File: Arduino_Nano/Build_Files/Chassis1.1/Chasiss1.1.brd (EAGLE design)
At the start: 50.8 x 38.1 mm, 11 parts, among them U2 LM7805

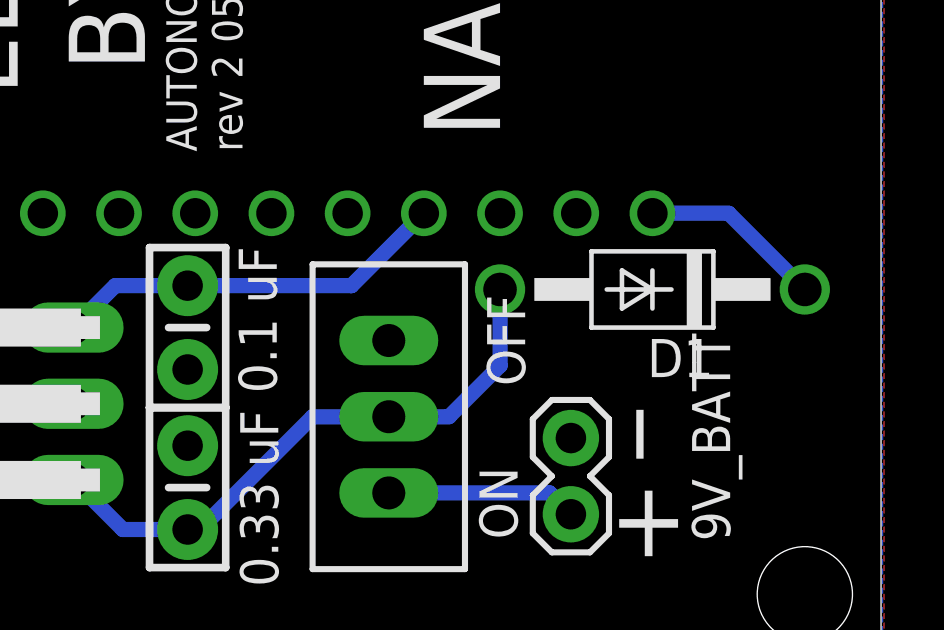
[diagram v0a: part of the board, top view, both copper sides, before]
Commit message: Fixed Issue with 3.3v regulator overpowering
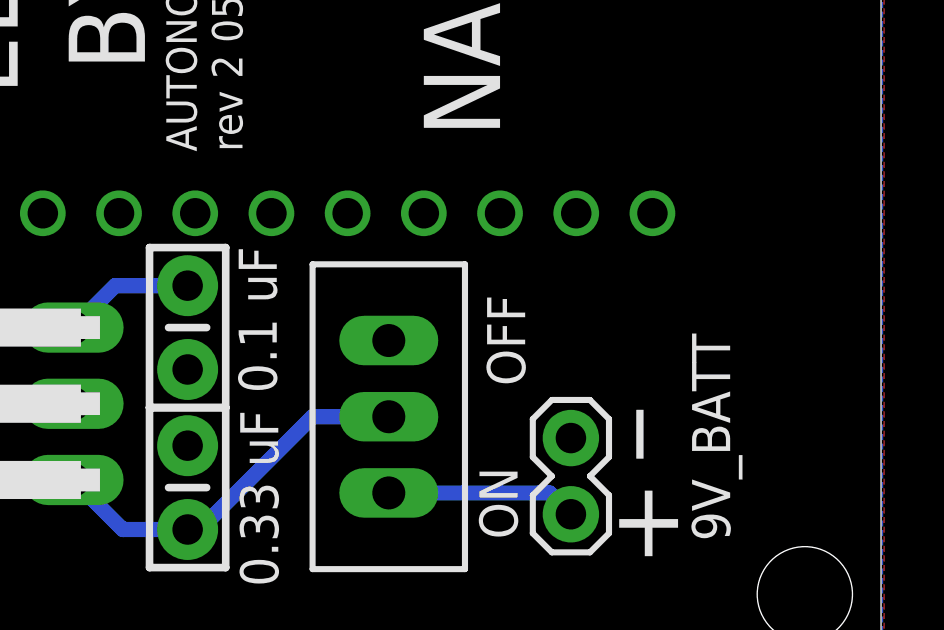
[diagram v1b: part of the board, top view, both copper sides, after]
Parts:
- removed D1: 1N4004, diode:DO41-10
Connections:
- removed net N$2: D1.C, NANO.30
- net 5V: no longer NANO.27
- net GND: no longer S1.1
- net VIN: no longer D1.A
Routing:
- net 5V: track 99.2 -> 90.3 mm
- net VIN: track 19.7 -> 12.8 mm
- net N$2: track 6.13 -> 0.00 mm
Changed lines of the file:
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@@
 <attribute name="POPULARITY" value="2" x="54.7116" y="51.6382" size="1.778" layer="27" rot="R270" display="off"/>
-</element>
-<element name="D1" library="diode" library_urn="urn:adsk.eagle:library:210" package="DO41-10" package3d_urn="urn:adsk.eagle:package:43336/1" value="1N4004" x="63.5" y="55.88" smashed="yes" rot="R180">
-<attribute name="NAME" x="65.532" y="54.229" size="1.27" layer="25" ratio="10" rot="R180"/>
-<attribute name="POPULARITY" value="82" x="63.5" y="55.88" size="1.778" layer="27" rot="R180" display="off"/>
-<attribute name="VALUE" x="65.532" y="58.674" size="1.27" layer="27" ratio="10" rot="R180"/>
 </element>
 </elements>
@@
 <wire x1="27.3304" y1="75.5904" x2="24.7904" y2="75.5904" width="0.508" layer="16"/>
 <wire x1="24.7904" y1="75.5904" x2="22.86" y2="73.66" width="0.508" layer="16"/>
-<contactref element="NANO" pad="27"/>
 <contactref element="HC-SR04" pad="4"/>
-<wire x1="48.006" y1="56.007" x2="53.467" y2="56.007" width="0.508" layer="16"/>
-<wire x1="53.467" y1="56.007" x2="55.88" y2="58.42" width="0.508" layer="16"/>
 <wire x1="49.53" y1="77.47" x2="49.53" y2="78.74" width="0.508" layer="16"/>
 <wire x1="49.53" y1="78.74" x2="50.8" y2="80.01" width="0.508" layer="16"/>
@@
 <vertex x="20.6502" y="43.4086"/>
 </polygon>
-<contactref element="S1" pad="1"/>
 </signal>
 <signal name="VIN">
@@
 <wire x1="52.1716" y1="51.6382" x2="48.41240625" y2="47.879" width="0.508" layer="16"/>
 <wire x1="48.41240625" y1="47.879" x2="48.006" y2="47.879" width="0.508" layer="16"/>
-<contactref element="D1" pad="A"/>
-<wire x1="54.7116" y1="51.6382" x2="56.7182" y2="51.6382" width="0.508" layer="16"/>
-<wire x1="56.7182" y1="51.6382" x2="58.42" y2="53.34" width="0.508" layer="16"/>
-<wire x1="58.42" y1="53.34" x2="58.42" y2="55.88" width="0.508" layer="16"/>
 </signal>
 <signal name="LEFT_SERVO">
@@
 <wire x1="54.7116" y1="49.0982" x2="60.071" y2="49.0982" width="0.508" layer="16"/>
 </signal>
-<signal name="N$2">
-<contactref element="NANO" pad="30"/>
-<contactref element="D1" pad="C"/>
-<wire x1="63.5" y1="58.42" x2="66.04" y2="58.42" width="0.508" layer="16"/>
-<wire x1="66.04" y1="58.42" x2="68.58" y2="55.88" width="0.508" layer="16"/>
-</signal>
 </signals>
 <mfgpreviewcolors>
@@
 which will not be processed correctly with this version.
 </note>
-<note version="8.2" severity="warning">
-Since Version 8.2, EAGLE supports online libraries. The ids
-of those online libraries will not be understood (or retained)
-with this version.
-</note>
-<note version="8.3" severity="warning">
-Since Version 8.3, EAGLE supports URNs for individual library
-assets (packages, symbols, and devices). The URNs of those assets
-will not be understood (or retained) with this version.
-</note>
-<note version="8.3" severity="warning">
-Since Version 8.3, EAGLE supports the association of 3D packages
-with devices in libraries, schematics, and board files. Those 3D
-packages will not be understood (or retained) with this version.
-</note>
 </compatibility>

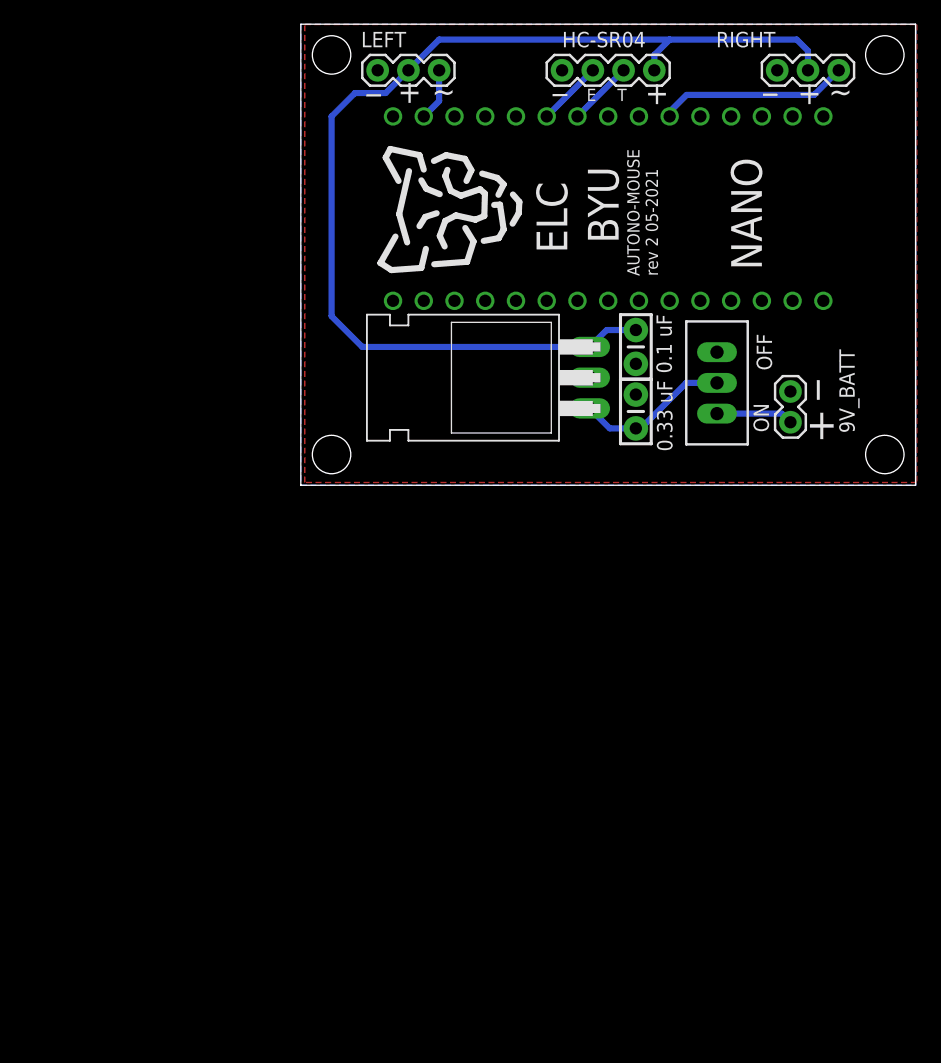
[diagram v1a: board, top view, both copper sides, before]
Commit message: Reverse diode not needed, routing was done incorrectly by accident. Also added route from voltage regulator to the Arduino Nano for power. Updated some notes in the README and cleaned out some unused files.
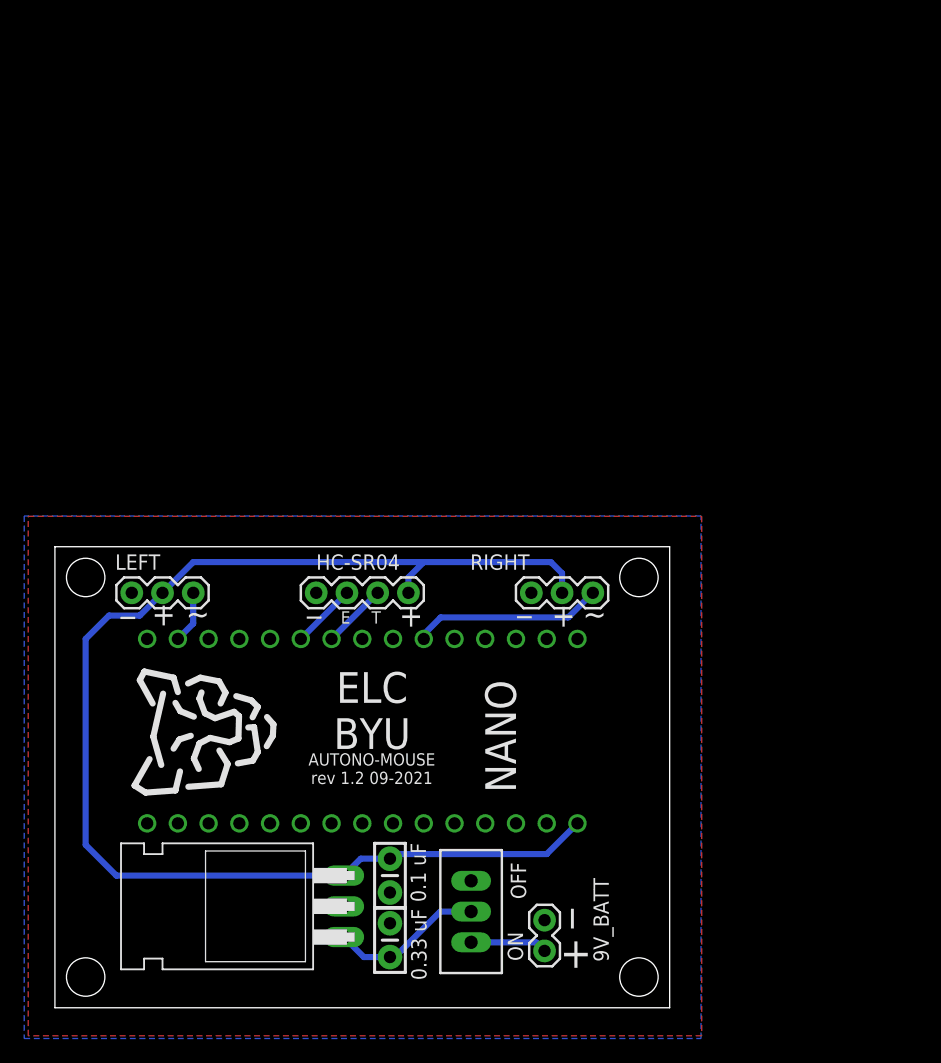
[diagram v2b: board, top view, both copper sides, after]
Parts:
- moved 9V_BATT 48.2 mm to (40.5, 7.24)
- moved C1 48.2 mm to (27.7, 5.59)
- moved C2 48.2 mm to (27.7, 10.9)
- moved U$1 48.2 mm to (8.20, 9.68)
- moved U2 48.2 mm to (13.7, 8.38)
- moved S1 48.2 mm to (34.4, 7.95)
- moved NANO 47.7 mm to (25.4, 22.9)
- moved HC-SR04 47.7 mm to (21.6, 34.3)
- moved LEFT 47.7 mm to (11.4, 34.3)
- moved RIGHT 47.7 mm to (44.5, 34.3)
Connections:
- net 5V: now also NANO.30
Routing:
- net 5V: track 90.3 -> 107.6 mm
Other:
- board text added: "AUTONO-MOUSE rev 1.2 09-2021"
- board text added: "ELC BYU"
- board text removed: "AUTONO-MOUSE rev 2 05-2021"
- board text removed: "BYU"
- board text removed: "ELC"
